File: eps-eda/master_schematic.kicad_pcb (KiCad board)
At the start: 2 copper layers, 96 x 90 mm, 80 parts, among them J1 USB_C_Receptacle, J2 436500212, J3 Conn_02x20_Odd_Even, J4 Conn_01x05_Female, U1 TPS61022RWUR, U2 TPS61022RWUR, U3 INA3221AIRGVR, U5 MAX77757JEFG435+, U6 MAX17055EWL+T, U7 ATA6560-GAQW-VAO, U8 PIC18F27Q84-E/SP

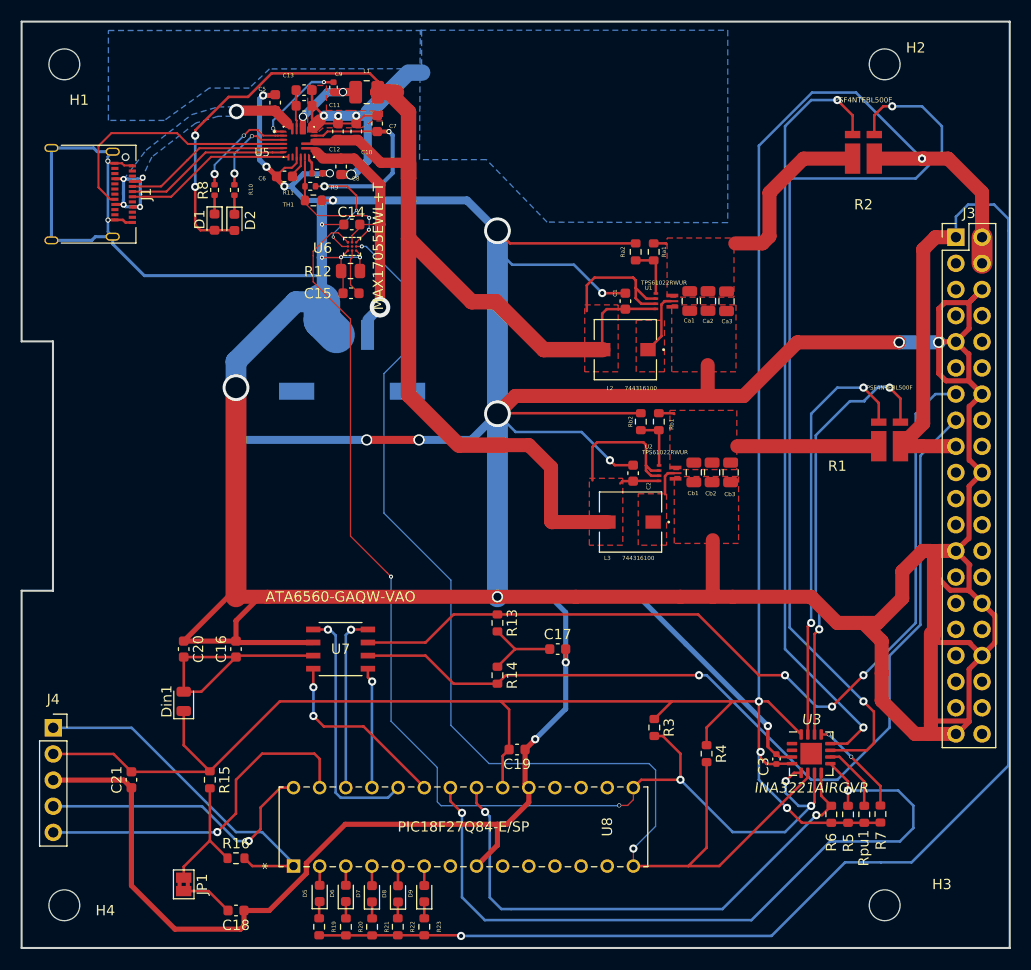
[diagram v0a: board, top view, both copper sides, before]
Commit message: rev 0.2 update
added 90deg pic adapter to include an edge cutout.

changed footprint of fuel gauge to implement ALRT signal.

rotated battery connector to better implement with the battery board.

Co-Authored-By: ajbrannigan <91212154+ajbrannigan@users.noreply.github.com>
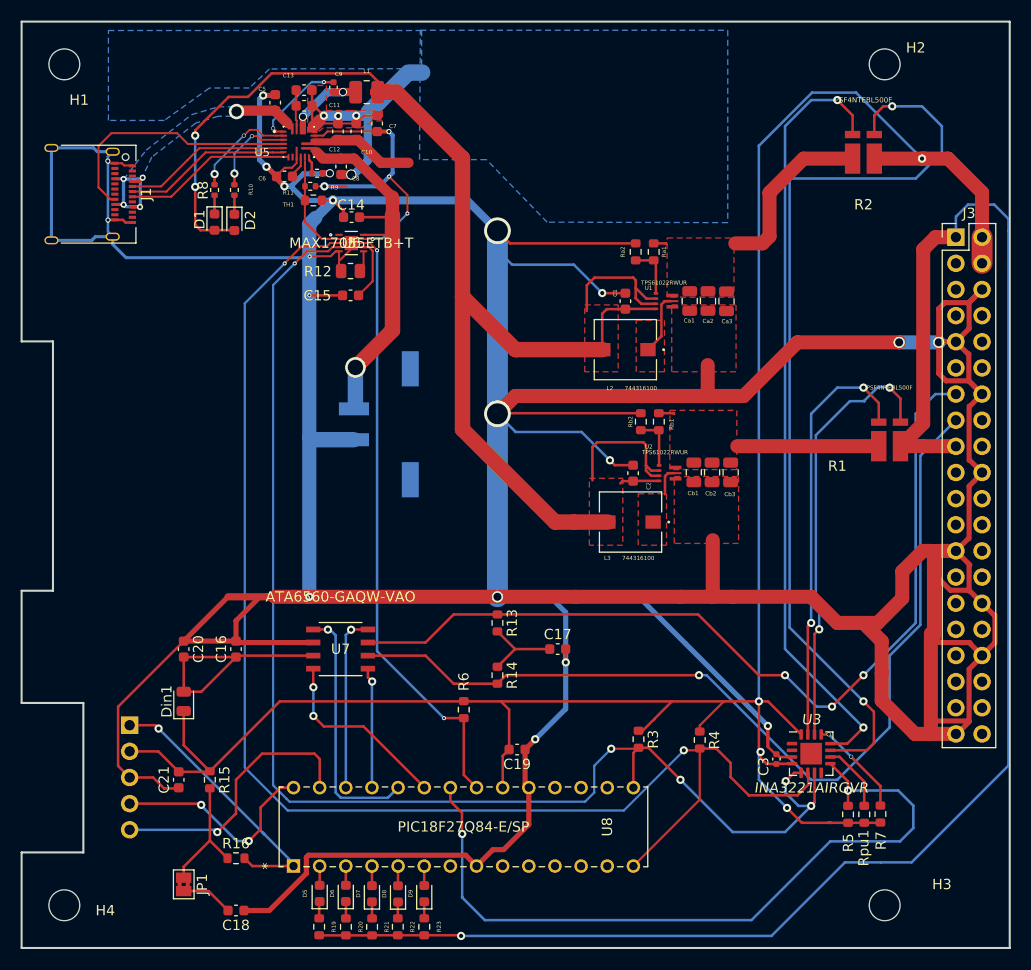
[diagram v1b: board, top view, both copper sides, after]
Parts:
- J4: value Conn_01x05_Female -> Conn_01x05_90deg; footprint Connector_PinSocket_2.54mm:PinSocket_1x05_P2.54mm_Vertical -> Connector_PinHeader_2.54mm:PinHeader_1x05_P2.54mm_Horizontal; moved to B.Cu
- U6: value MAX17055EWL+T -> MAX17055ETB+T; footprint max17055:MAX17055EWL_plus_T -> max17055 smd:MAX17055ETB&plus_T
- moved R6 37.1 mm to (80.5, 122.7), turned to -90 degrees
- moved J4 7.43 mm to (48.1, 124.2), turned to 180 degrees
- moved J2 6.39 mm to (75.0, 95.0), turned to -90 degrees
- moved C21 4.60 mm to (52.9, 129.5)
- moved R3 1.91 mm to (97.5, 125.6)
- moved R4 1.48 mm to (103.5, 125.7)
- moved C14 0.71 mm to (69.6, 74.9)
- moved U6 0.34 mm to (69.6, 77.4), turned to 0 degrees
- moved C15 0.21 mm to (69.5, 82.5)
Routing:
- net GND: track 699.8 -> 651.0 mm, vias 24 -> 20
- net /ColoradoCUBE_Payload/SCL_RC3: track 116.2 -> 134.5 mm
- net /charge schem/SYSPOWER: track 171.7 -> 158.1 mm
- net /ColoradoCUBE_Payload/SDA_RC4: track 119.4 -> 131.2 mm
- net /charge schem/V_BAT: track 26.5 -> 36.7 mm
- net /ColoradoCUBE_Payload/ICSPD: track 28.1 -> 20.7 mm, vias 1 -> 2
- net /ColoradoCUBE_Payload/ICSPC: track 34.0 -> 26.7 mm
- net /ColoradoCUBE_Payload/MCLR: track 34.1 -> 27.1 mm, vias 0 -> 1
- net /ColoradoCUBE_Payload/ALRT: track 52.2 -> 59.0 mm
- net /ColoradoCUBE_Payload/5V: track 220.6 -> 213.9 mm
- net Net-(R11-Pad2): track 13.7 -> 10.2 mm, vias 2 -> 0
- net Net-(C7-Pad1): track 29.7 -> 31.3 mm, vias 4 -> 5
- net Net-(C15-Pad1): track 4.49 -> 5.92 mm
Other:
- outline, holes or cut-outs redrawn

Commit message: EPS V0.2
Adjusted placement of resistors R19 through R23, and capacitor C18. For mounting purposes. Most DRC errors have now been cleared.
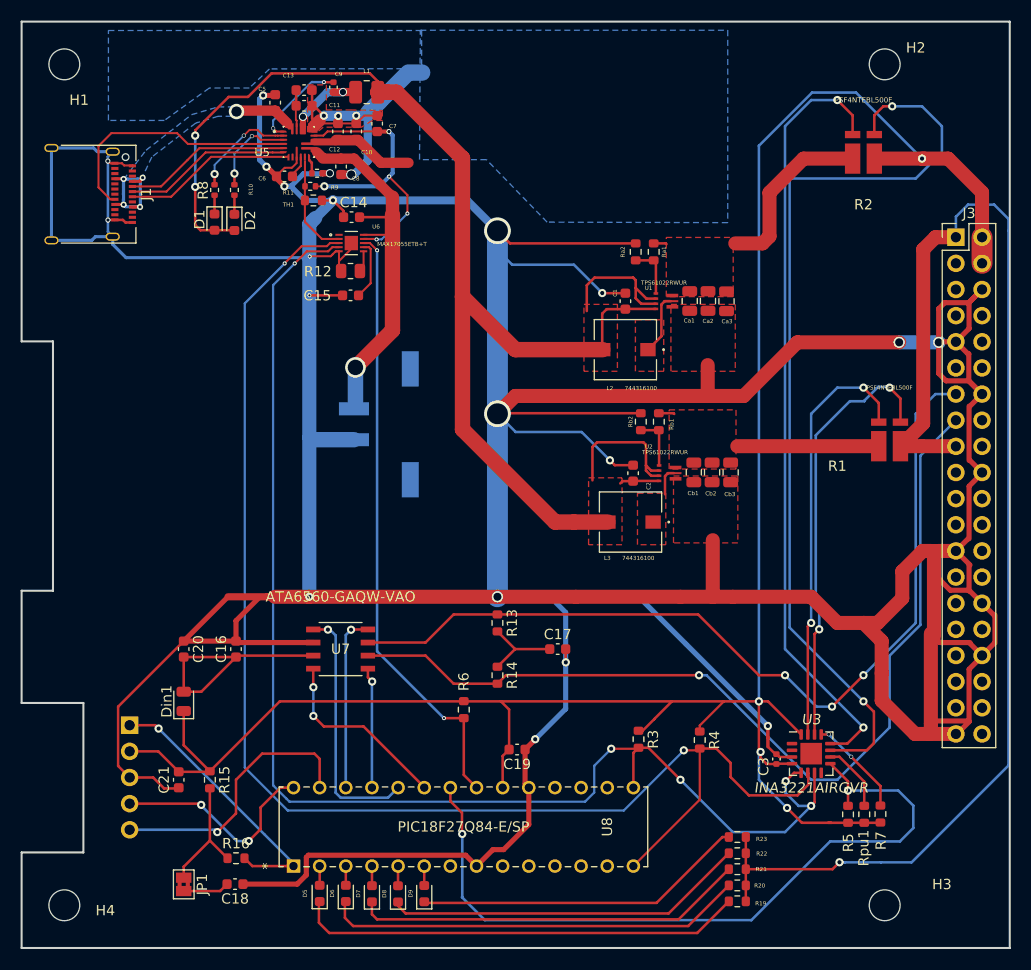
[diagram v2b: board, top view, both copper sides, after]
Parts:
- moved R19 40.7 mm to (107.1, 141.3), turned to 0 degrees
- moved R20 38.2 mm to (107.1, 139.8), turned to 0 degrees
- moved R21 35.9 mm to (107.1, 138.2), turned to 0 degrees
- moved R22 33.7 mm to (107.1, 136.7), turned to 0 degrees
- moved R23 31.6 mm to (107.1, 135.1), turned to 0 degrees
- moved C18 2.57 mm to (58.3, 139.7)
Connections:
- U3 pad 9: /converterschematic/CRT -> /ColoradoCUBE_Payload/CRT
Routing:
- net Net-(D5-Pad1): track 1.65 -> 43.6 mm
- net Net-(D6-Pad1): track 1.64 -> 40.8 mm
- net /ColoradoCUBE_Payload/3.3V: track 164.2 -> 126.3 mm
- net Net-(D7-Pad1): track 1.61 -> 38.1 mm
- net Net-(D8-Pad1): track 1.60 -> 35.2 mm
- net Net-(D9-Pad1): track 1.61 -> 32.3 mm
- net Net-(C7-Pad1): track 31.3 -> 29.1 mm
- net GND: track 651.0 -> 650.1 mm
- net Net-(C18-Pad2): track 5.09 -> 4.49 mm

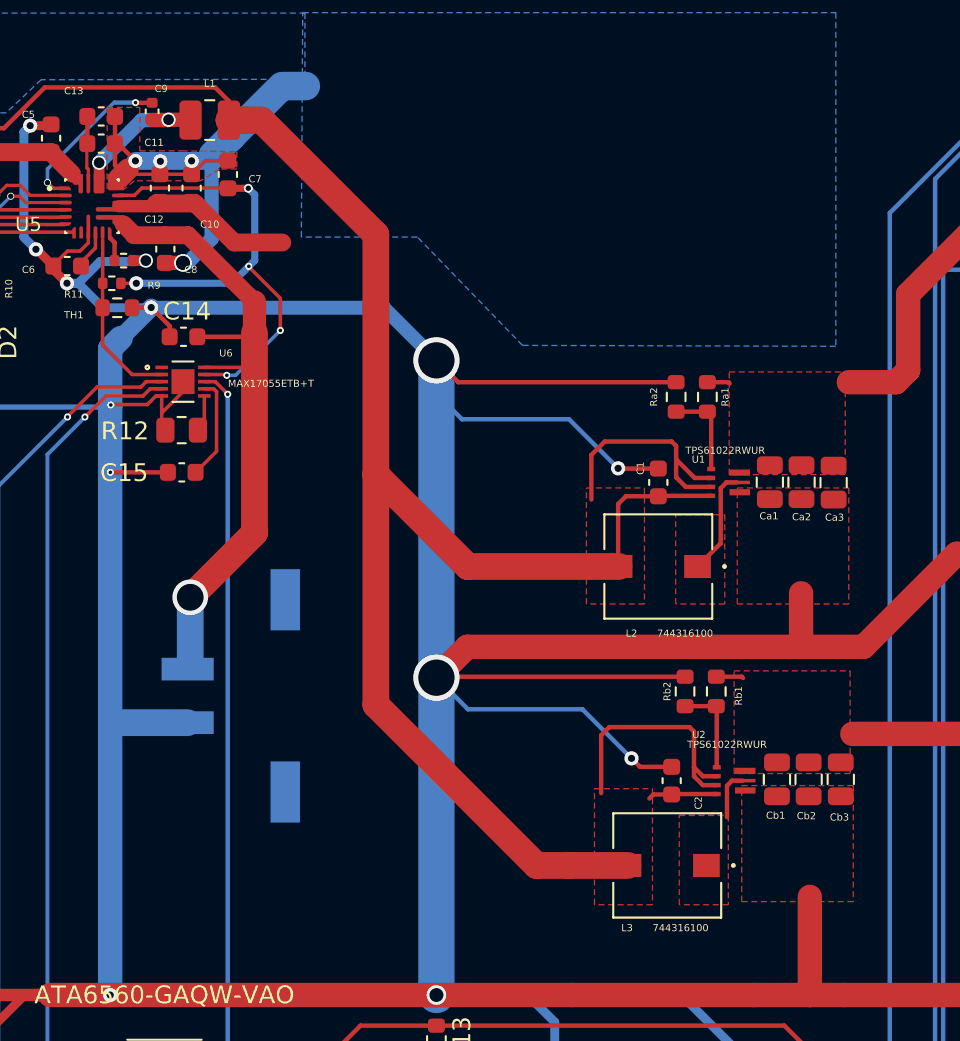
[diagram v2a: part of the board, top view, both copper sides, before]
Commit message: EPS V0.2 quick update
added schottyky diode before 3.3V boost converter
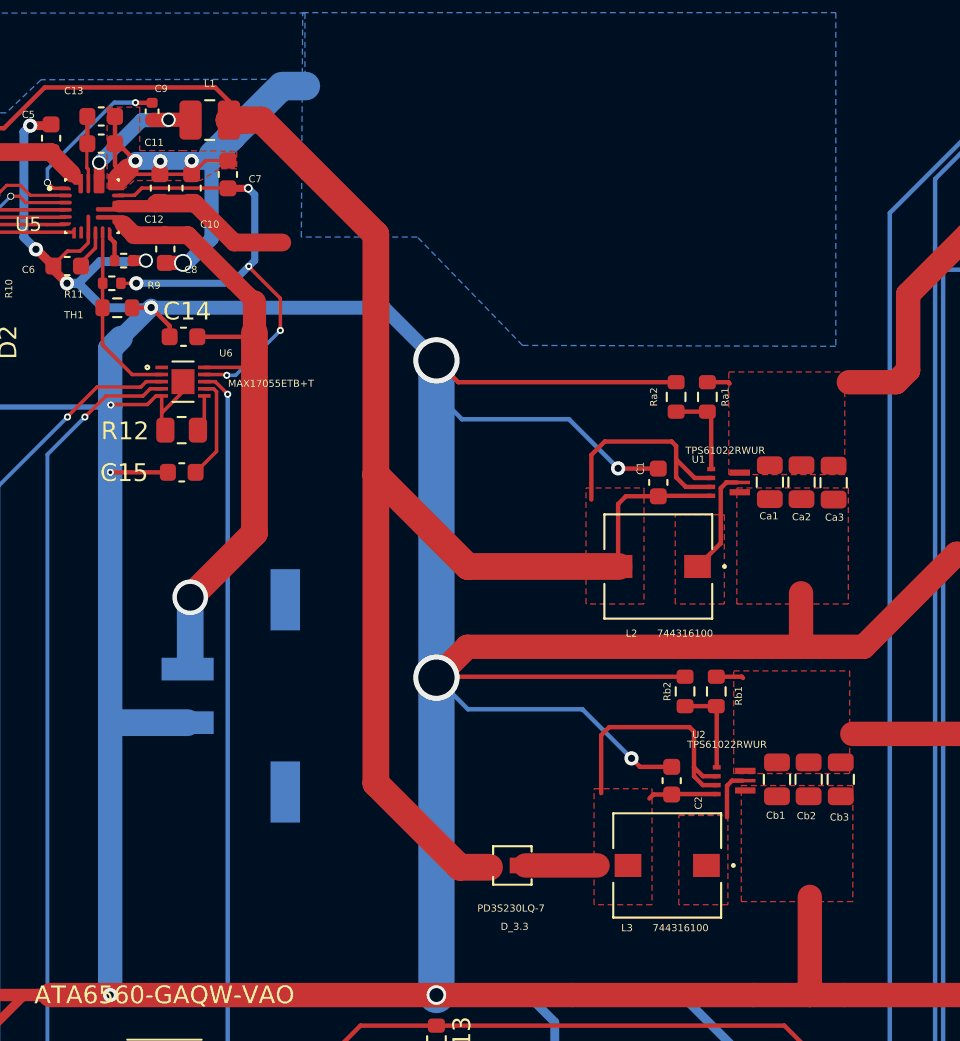
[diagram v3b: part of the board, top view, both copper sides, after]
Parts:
- added D_3.3: PD3S230LQ-7, footprints3:PD3S230LQ-7, F.Cu at (88.1, 104.5)
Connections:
- C2 pad 1: /charge schem/SYSPOWER -> Net-(L3-Pad2)
- L3 pad 2: /charge schem/SYSPOWER -> Net-(L3-Pad2)
- U2 pad 5: /charge schem/SYSPOWER -> Net-(L3-Pad2)
- U2 pad 6: /charge schem/SYSPOWER -> Net-(L3-Pad2)
- U2 pad 7: /charge schem/SYSPOWER -> Net-(L3-Pad2)
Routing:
- net /charge schem/SYSPOWER: track 158.1 -> 134.9 mm
- net Net-(L3-Pad2): track 0.00 -> 22.1 mm
- added copper zone on F.Cu, net Net-(L3-Pad2)

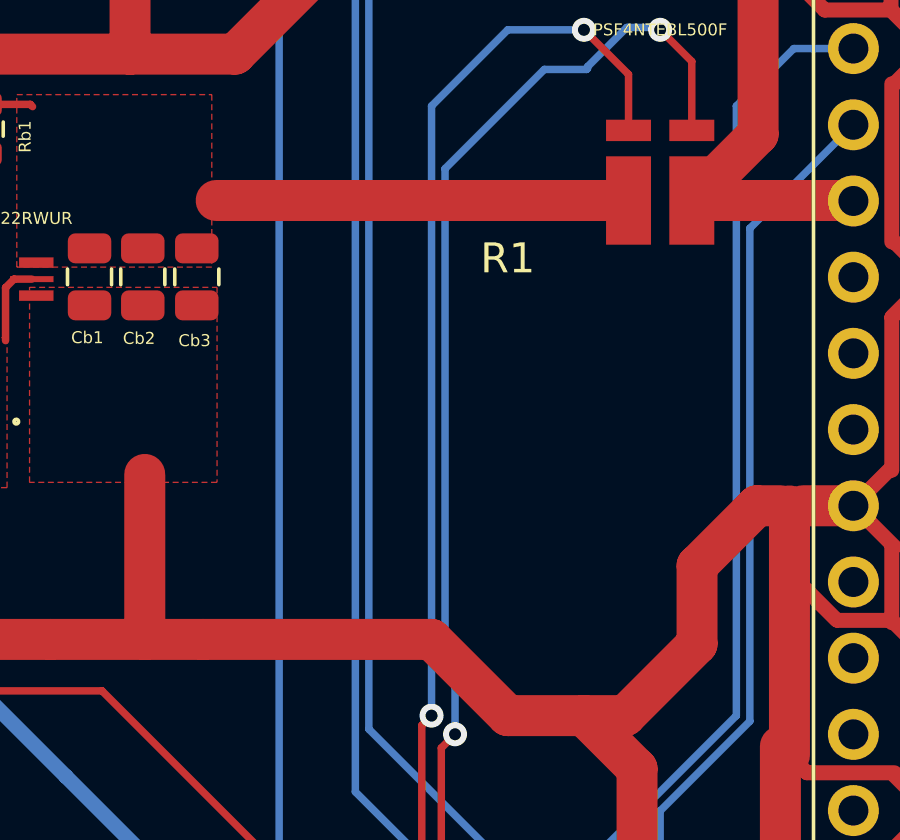
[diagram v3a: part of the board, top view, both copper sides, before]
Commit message: EPS V0.3
Added over voltage protection system for the 3.3V rail.
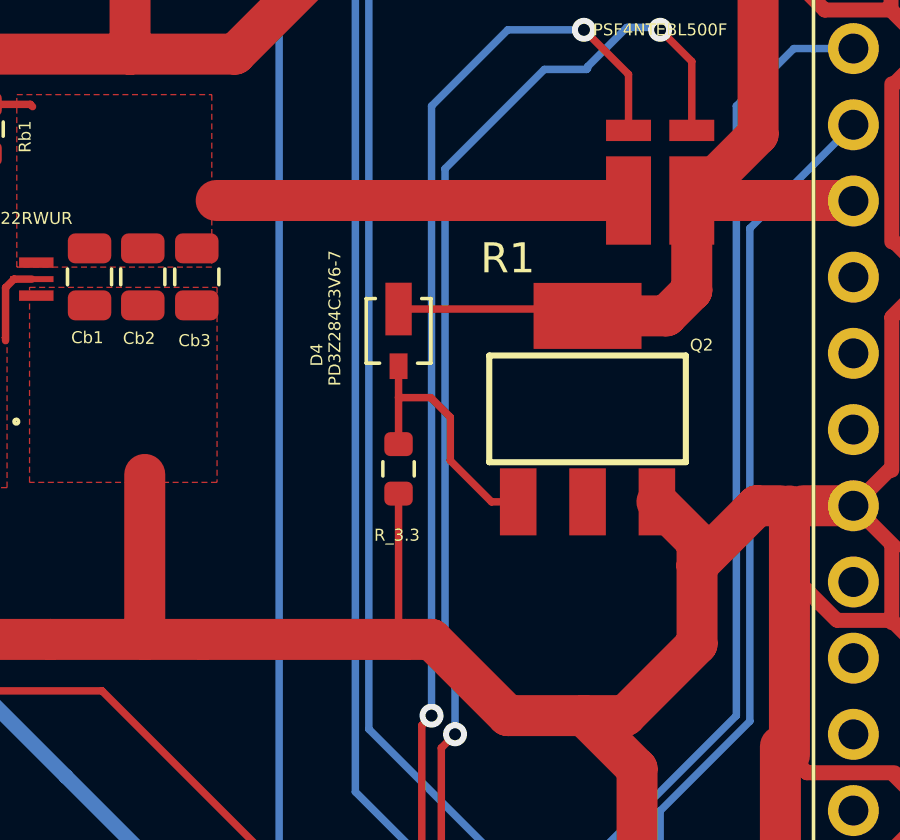
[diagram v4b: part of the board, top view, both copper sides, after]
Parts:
- added D4: PD3Z284C3V6-7, zener_ovp:PD3Z284C3V6-7, F.Cu at (113.2, 101.5)
- added Q2: FZT688BTA, fzt688bta_footprint:SOT230P700X180-4N, F.Cu at (119.5, 104.1)
- added R_3.3: 1k, Resistor_SMD:R_0603_1608Metric, F.Cu at (113.2, 106.1)
- Cb1, Cb2, Cb3: value 5uF -> 22uF
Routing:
- net /ColoradoCUBE_Payload/3.3V: track 126.3 -> 139.5 mm
- net Net-(D4-Pad2): track 0.00 -> 8.87 mm
- net GND: track 650.1 -> 657.7 mm
